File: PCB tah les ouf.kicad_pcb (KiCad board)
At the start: 2 copper layers, 60 x 60 mm, 2 parts, among them J1 USB_C_Receptacle_USB2.0_16P, U1 ESP32-S3-WROOM-1

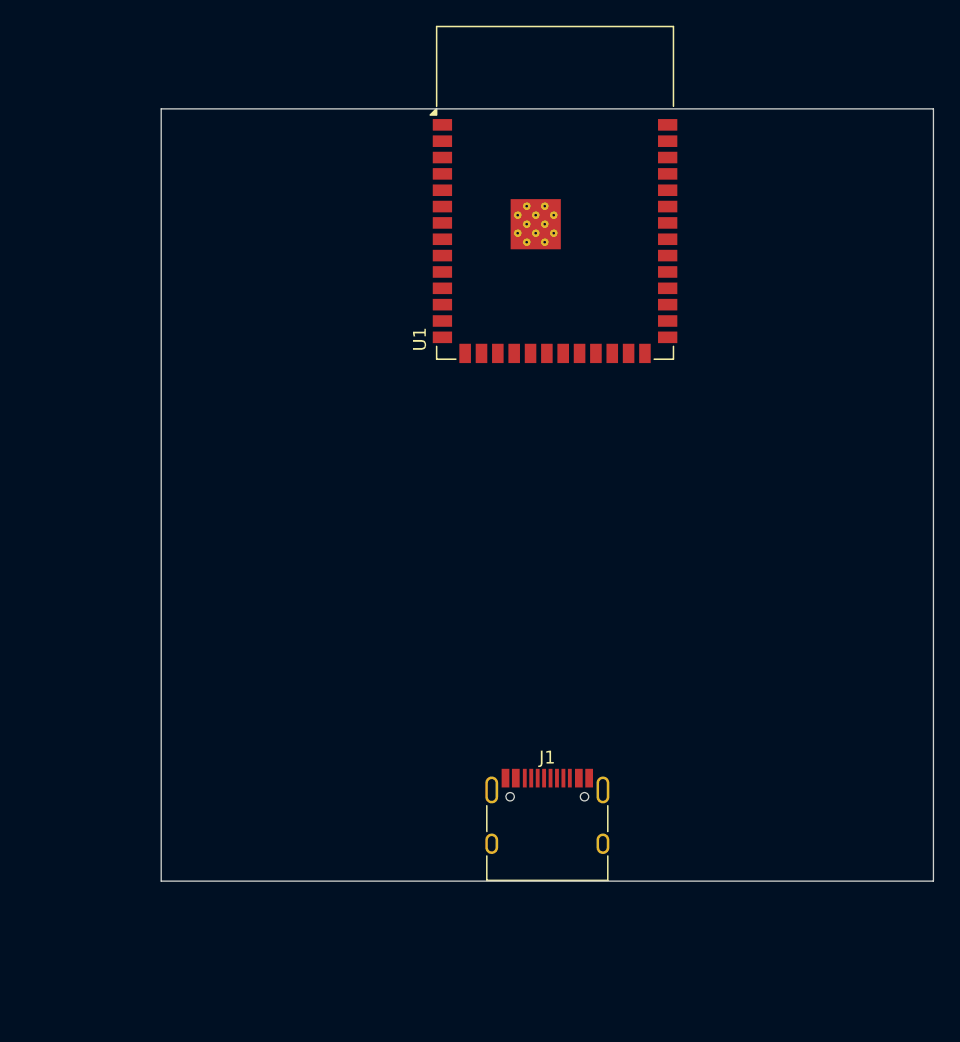
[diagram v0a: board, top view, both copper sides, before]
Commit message: Ajout ESP32-S3-WROOM-1U
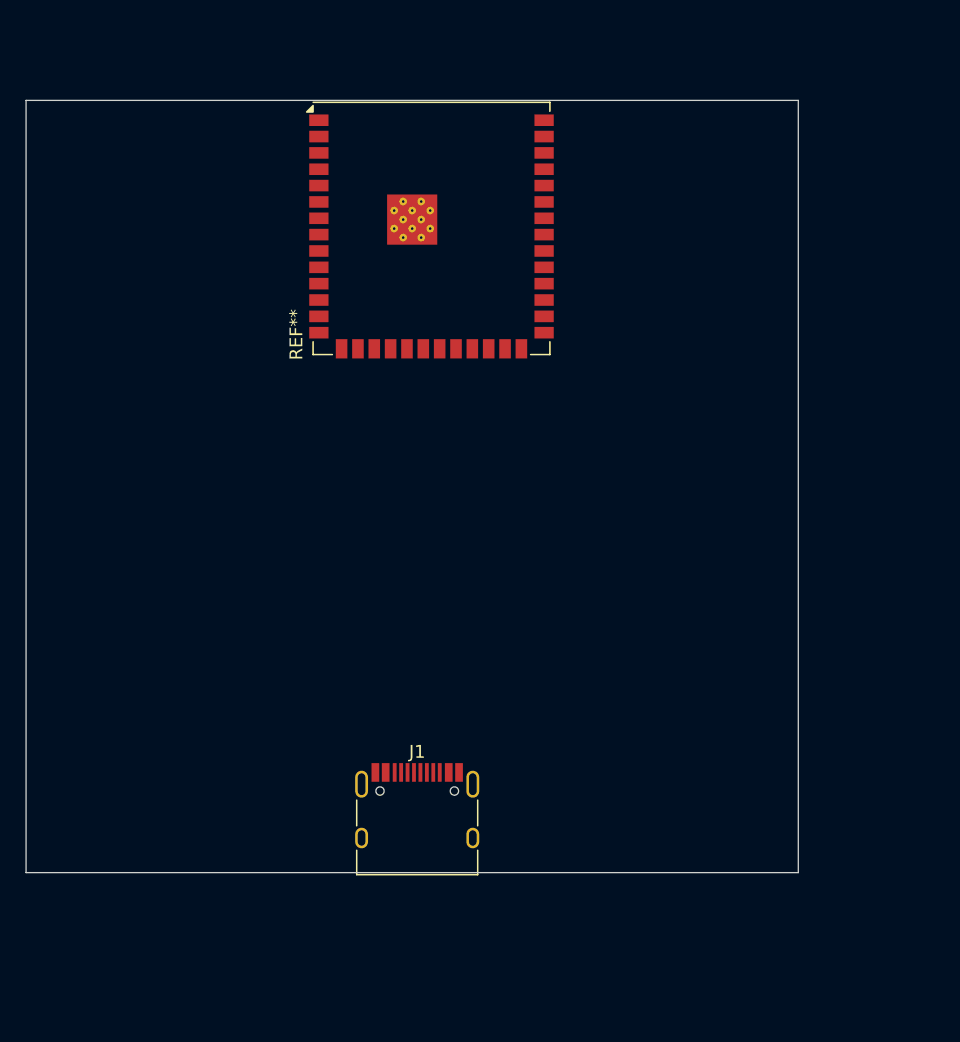
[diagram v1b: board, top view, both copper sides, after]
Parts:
- removed U1: ESP32-S3-WROOM-1, RF_Module:ESP32-S3-WROOM-1
- added REF**: ESP32-S3-WROOM-1U, RF_Module:ESP32-S3-WROOM-1U, F.Cu at (120.5, 59.8)
- moved J1 10.1 mm to (119.4, 106.1)

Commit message: Ajustement TMC
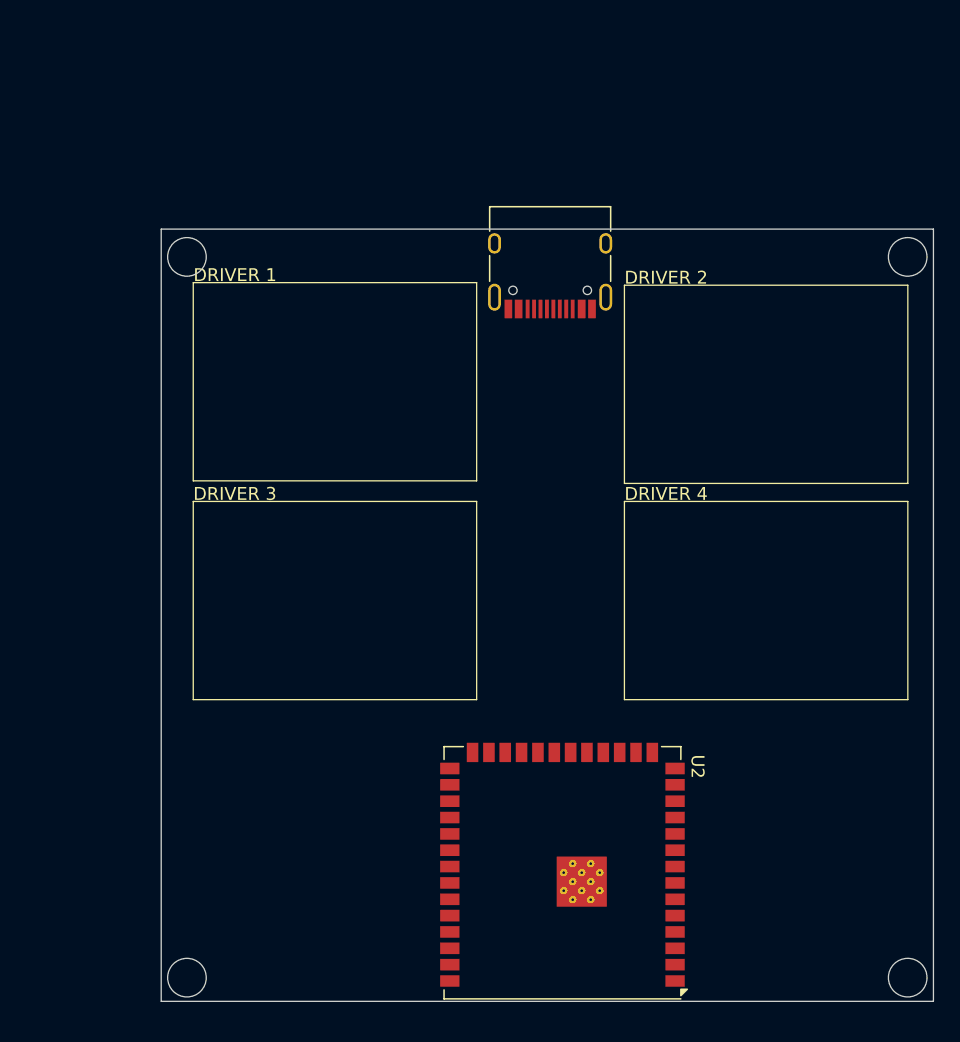
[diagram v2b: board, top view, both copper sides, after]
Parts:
- removed REF**: ESP32-S3-WROOM-1U, RF_Module:ESP32-S3-WROOM-1U
- added U2: ESP32-S3-WROOM-1, RF_Module:ESP32-S3-WROOM-1U, F.Cu at (130.7, 109.8)
- moved J1 45.3 mm to (129.7, 62.0), turned to 180 degrees
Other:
- outline, holes or cut-outs redrawn
- board text added: "DRIVER 1"
- board text added: "DRIVER 2"
- board text added: "DRIVER 3"
- board text added: "DRIVER 4"

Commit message: AJOUT driver stepper
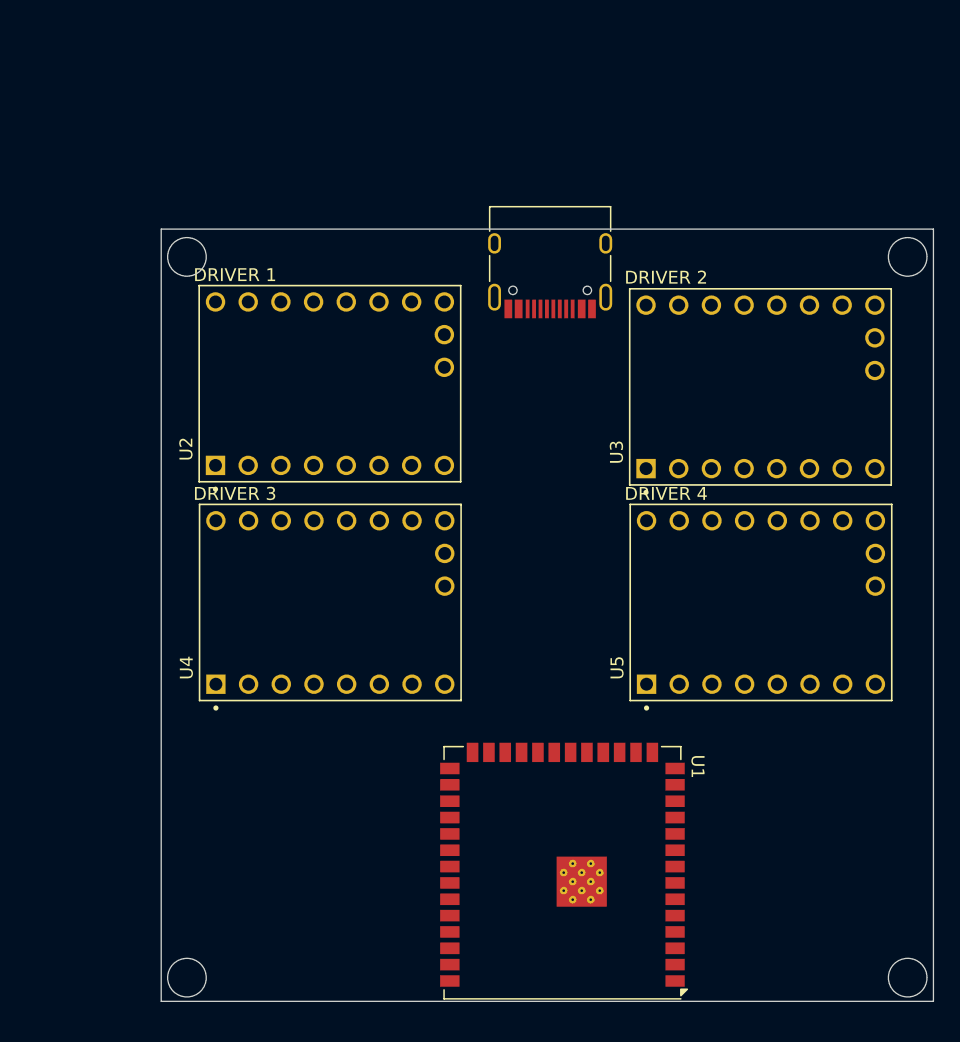
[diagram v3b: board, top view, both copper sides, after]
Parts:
- added U2: TMC2209_SILENTSTEPSTICK, TMC2209:MODULE_TMC2209_SILENTSTEPSTICK, F.Cu at (112.6, 71.8)
- added U3: TMC2209_SILENTSTEPSTICK, TMC2209:MODULE_TMC2209_SILENTSTEPSTICK, F.Cu at (146.1, 72.1)
- added U4: TMC2209_SILENTSTEPSTICK, TMC2209:MODULE_TMC2209_SILENTSTEPSTICK, F.Cu at (112.6, 88.8)
- added U5: TMC2209_SILENTSTEPSTICK, TMC2209:MODULE_TMC2209_SILENTSTEPSTICK, F.Cu at (146.1, 88.8)
- renumbered U2 to U1
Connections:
- U1 pad 1: Net-(U2-GND-Pad1) -> GND
- U1 pad 3: unconnected-(U2-EN-Pad3) -> /ESP32_EN
- U1 pad 40: Net-(U2-GND-Pad1) -> GND
- U1 pad 41: Net-(U2-GND-Pad1) -> GND

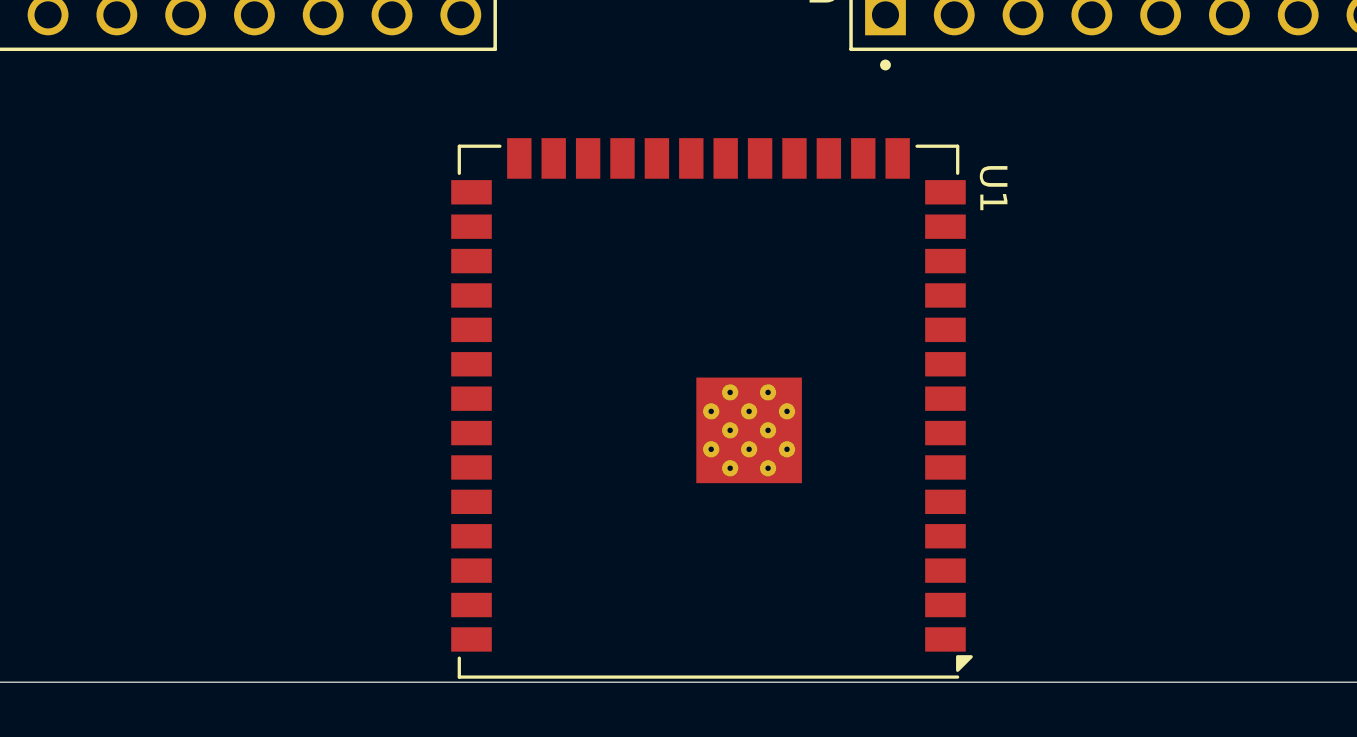
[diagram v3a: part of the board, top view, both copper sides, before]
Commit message: Fix problem / ESD Protection
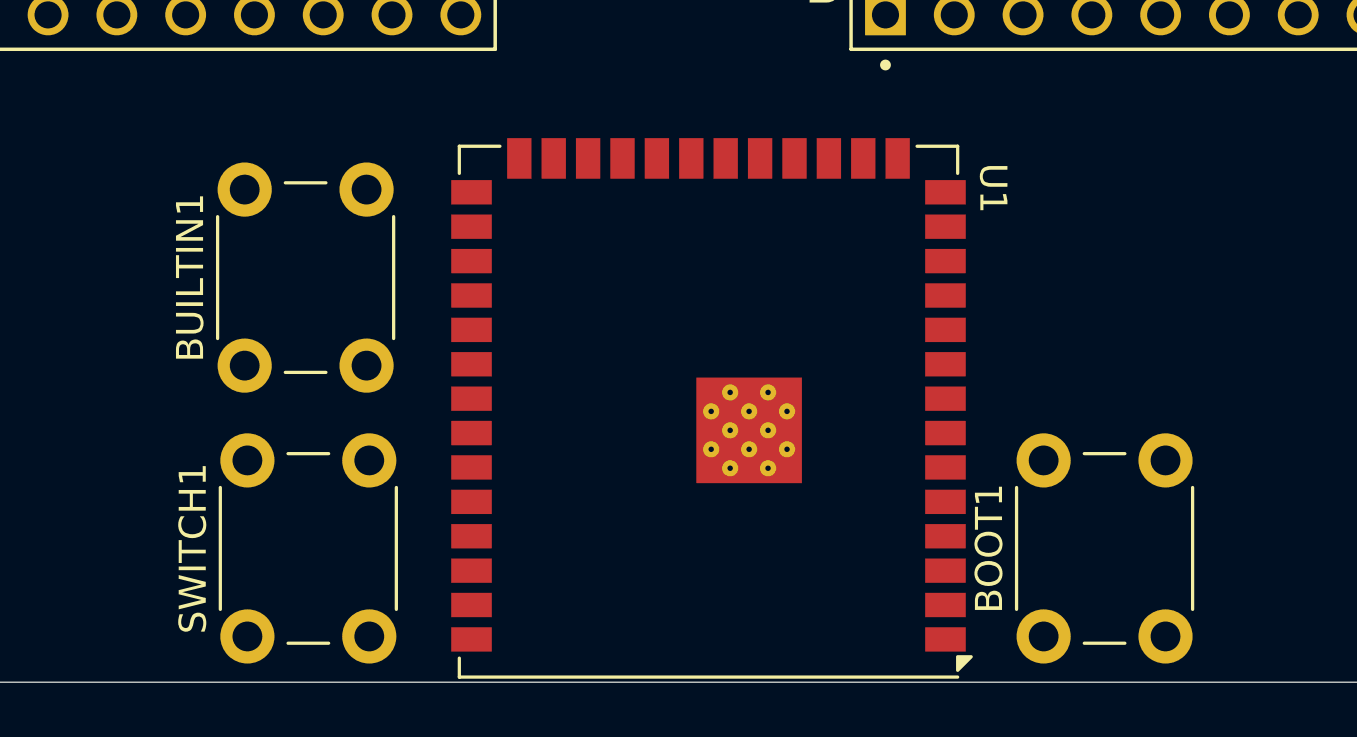
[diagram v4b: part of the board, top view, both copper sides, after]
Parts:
- added BOOT1: SW_MEC_5E, Button_Switch_THT:SW_PUSH_6mm_H4.3mm, F.Cu at (143.1, 118.2)
- added BUILTIN1: SW_MEC_5E, Button_Switch_THT:SW_PUSH_6mm_H4.3mm, F.Cu at (113.5, 108.2)
- added SWITCH1: SW_MEC_5E, Button_Switch_THT:SW_PUSH_6mm_H4.3mm, F.Cu at (113.7, 118.2)
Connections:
- J1 pad S1: unconnected-(J1-SHIELD-PadS1)_2 -> GND
- U1 pad 27: unconnected-(U1-IO0-Pad27) -> /GPIO0

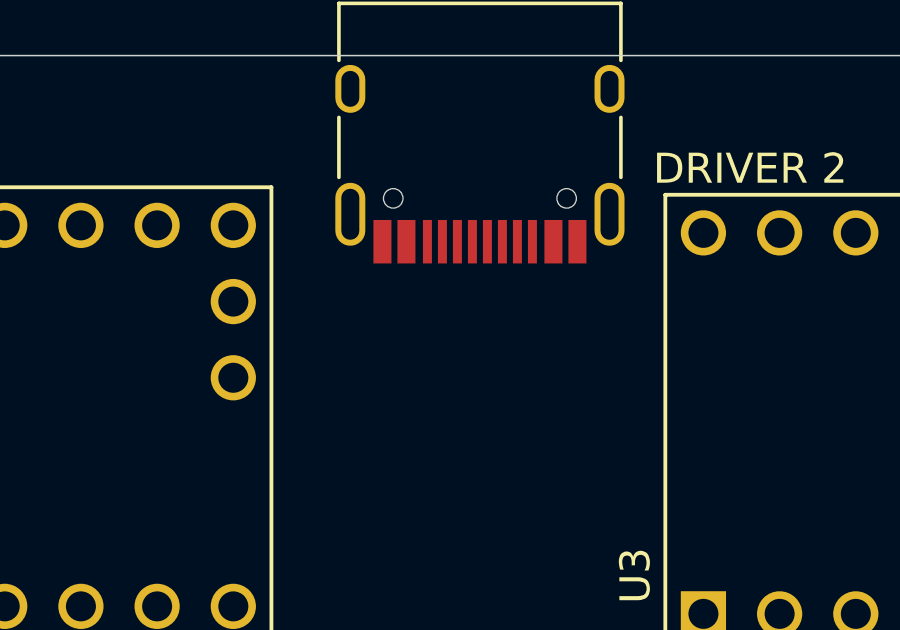
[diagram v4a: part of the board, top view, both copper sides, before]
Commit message: correction problemes
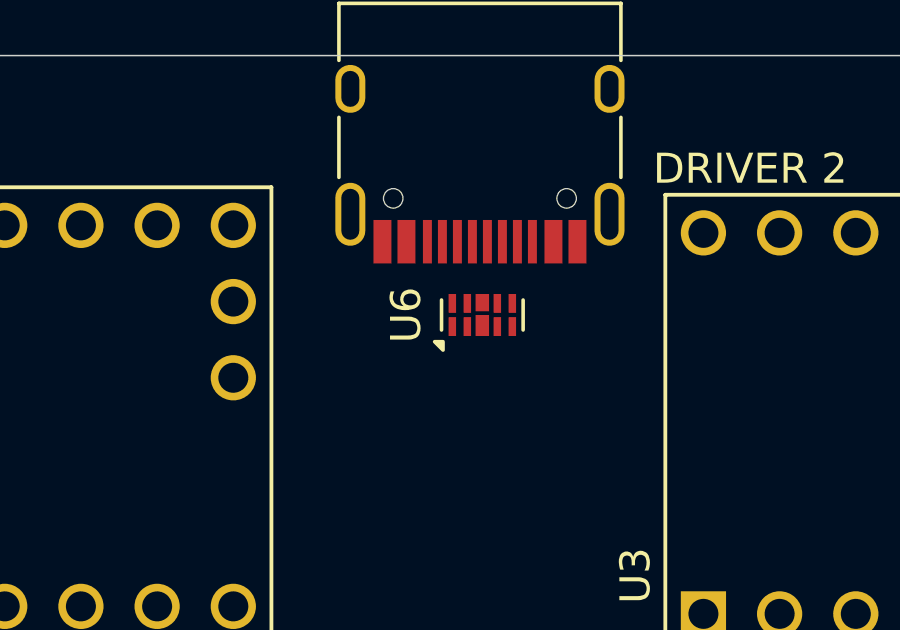
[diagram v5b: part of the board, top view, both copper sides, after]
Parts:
- added U6: D3V3XA4B10LP, Package_DFN_QFN:Diodes_UDFN-10_1.0x2.5mm_P0.5mm, F.Cu at (129.8, 68.5)

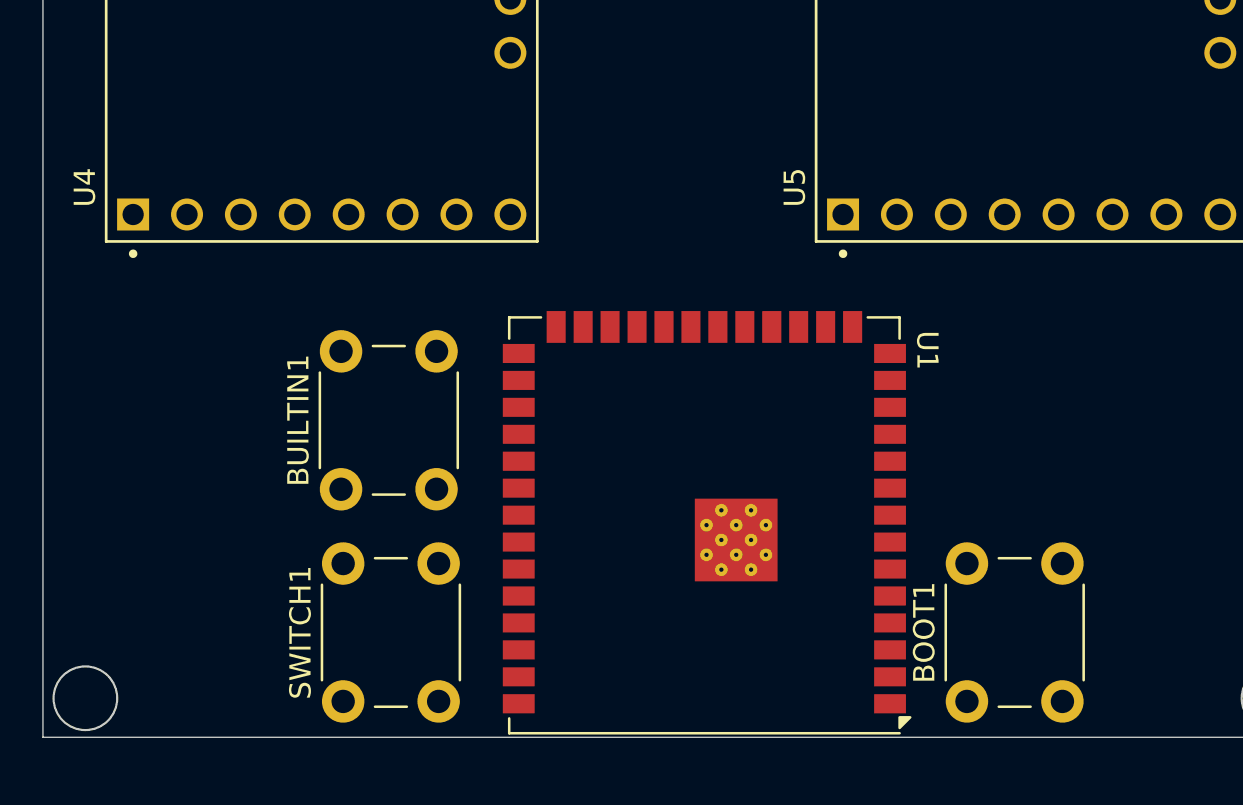
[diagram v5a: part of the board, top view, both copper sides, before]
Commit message: Ajout Auto flash mode
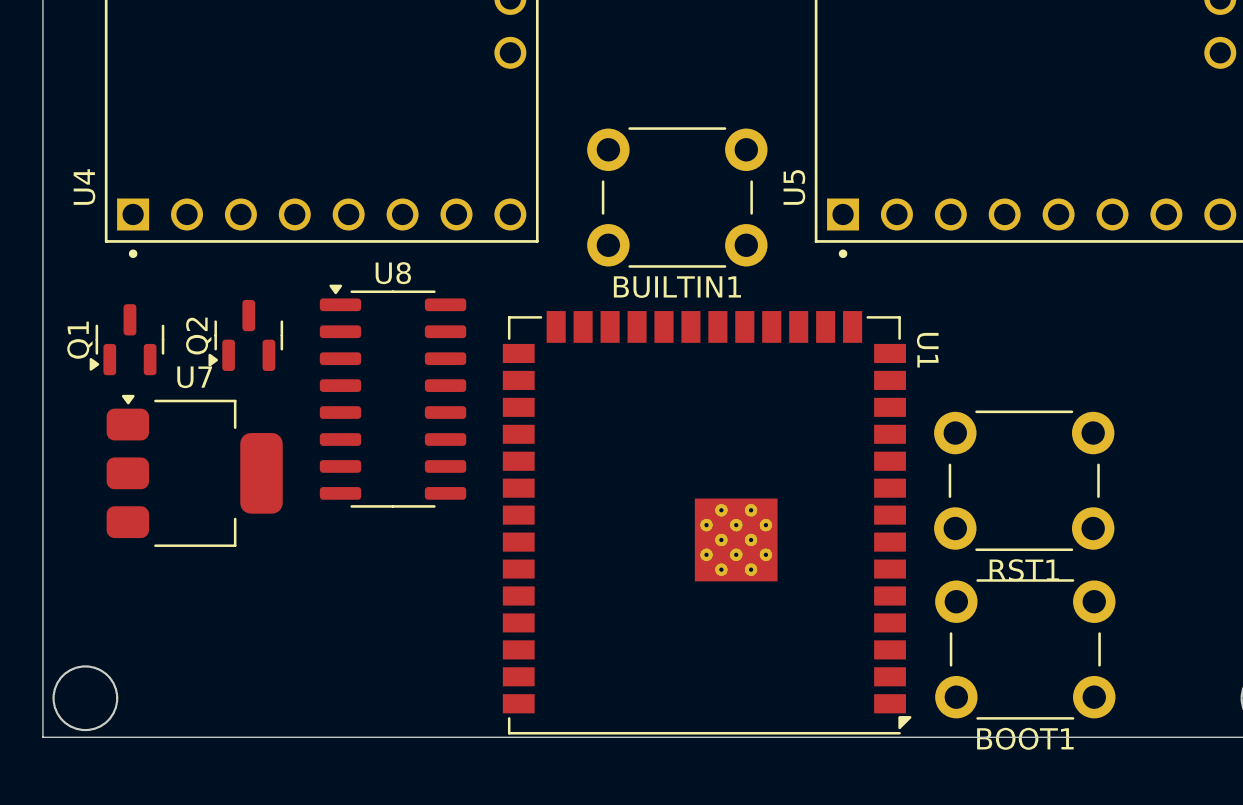
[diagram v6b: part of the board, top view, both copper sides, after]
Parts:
- added Q1: 2N7002, Package_TO_SOT_SMD:SOT-23, F.Cu at (103.6, 101.1)
- added Q2: 2N7002, Package_TO_SOT_SMD:SOT-23, F.Cu at (109.2, 100.9)
- added U7: AMS1117-3.3, Package_TO_SOT_SMD:SOT-223-3_TabPin2, F.Cu at (106.7, 107.4)
- added U8: CH340C, Package_SO:SOIC-16_3.9x9.9mm_P1.27mm, F.Cu at (116.0, 103.9)
- moved RST1 36.3 mm to (149.0, 110.0), turned to 180 degrees
- moved BUILTIN1 22.3 mm to (132.7, 96.7), turned to 180 degrees
- moved BOOT1 6.00 mm to (149.1, 118.0), turned to 180 degrees
- renumbered SWITCH1 to RST1
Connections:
- BUILTIN1 pad 1: unconnected-(BUILTIN1-Pad1) -> GND
- BUILTIN1 pad 2: unconnected-(BUILTIN1-Pad2) -> GND
- J1 pad A6: /D_P -> /USB_P
- J1 pad A7: /D_N -> /USB_N
- J1 pad B6: /D_P -> /USB_P
- J1 pad B7: /D_N -> /USB_N
- U1 pad 13: unconnected-(U1-IO19-Pad13) -> /USB_N
- U1 pad 14: unconnected-(U1-IO20-Pad14) -> /USB_P
- U1 pad 2: unconnected-(U1-3V3-Pad2) -> /3V3
- U1 pad 36: unconnected-(U1-RXD0-Pad36) -> /UART_RX
- U1 pad 37: unconnected-(U1-TXD0-Pad37) -> /UART_TX
- U6 pad 1: /D_N -> /USB_N
- U6 pad 10: /D_N -> /USB_N
- U6 pad 2: /D_P -> /USB_P
- U6 pad 9: /D_P -> /USB_P
